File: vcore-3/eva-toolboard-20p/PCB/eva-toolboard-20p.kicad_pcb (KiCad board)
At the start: 2 copper layers, 44.1 x 48.8 mm, 12 parts, among them J1 TH0, J2 HEATER, J3 STEPPER, J4 Main connector, J5 HOTENDFAN, J6 PARTFAN_1, J7 PARTFAN_2, J8 ENDSTOP_X, J9 PROBE

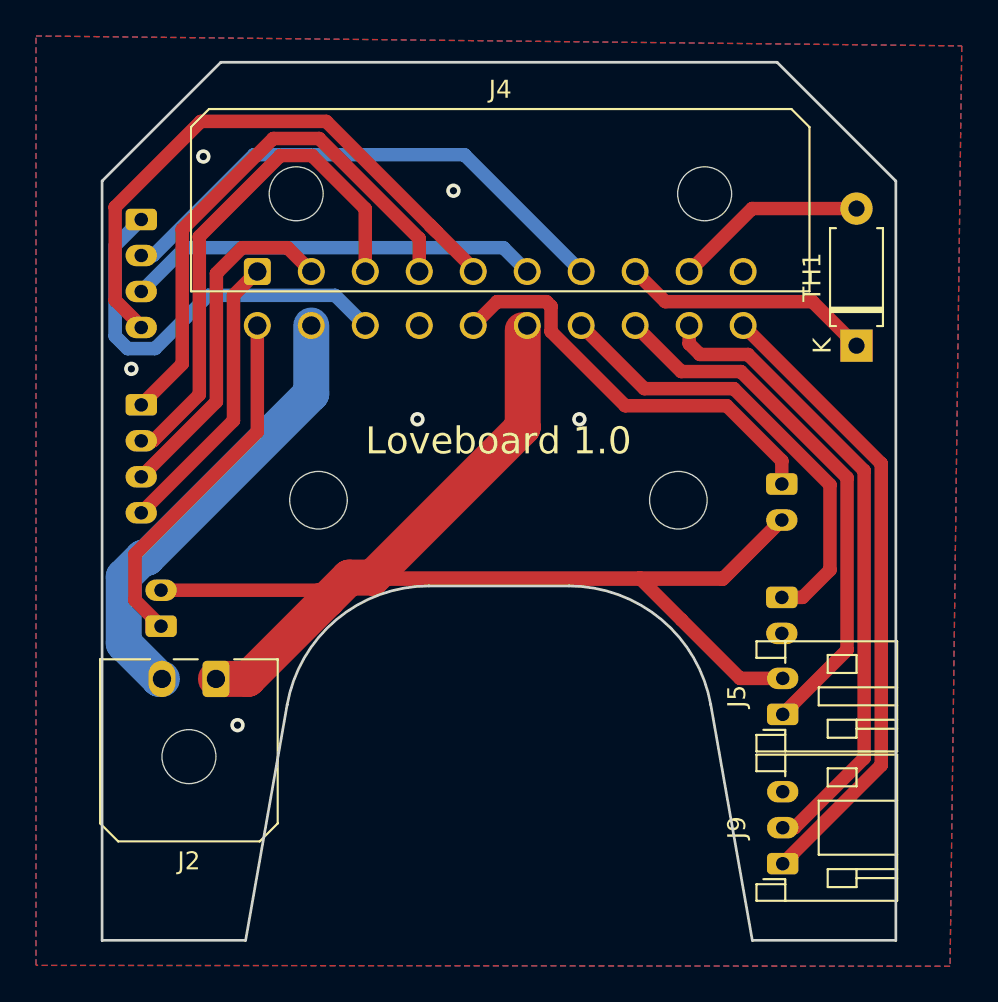
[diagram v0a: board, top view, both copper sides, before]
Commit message: Added and moved connector labels
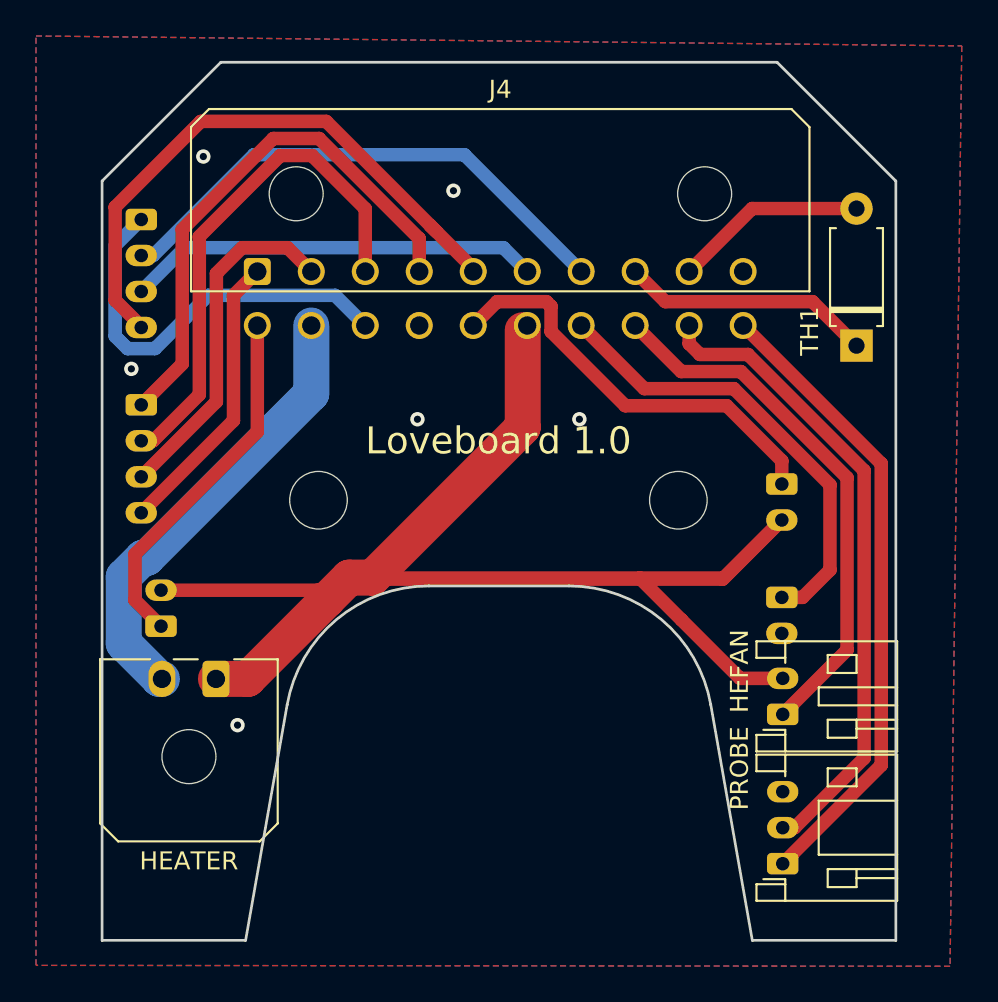
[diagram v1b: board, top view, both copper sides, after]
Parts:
- renumbered J8 to E_X, J2 to HEATER, J5 to HEFAN, J6 to PFAN1, J7 to PFAN2, J9 to PROBE, J3 to STEPPER, J1 to TH0
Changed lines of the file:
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@@
     (property "Sheetname" "")
     (attr through_hole)
-    (fp_text reference "J9" (at 2 -2.55 90) (layer "F.SilkS")
+    (fp_text reference "PROBE" (at 5.3 -2.4 90) (layer "F.SilkS")
       (effects (font (size 1 1) (thickness 0.15)))
     )
@@
     (property "Sheetname" "")
     (attr through_hole)
-    (fp_text reference "J2" (at 1.5 -10.12) (layer "F.SilkS")
+    (fp_text reference "HEATER" (at 1.5 -10.12) (layer "F.SilkS")
       (effects (font (size 1 1) (thickness 0.15)))
     )
@@
     (property "Sheetname" "")
     (attr through_hole)
-    (fp_text reference "TH1" (at 3.81 -2.47 90) (layer "F.SilkS")
+    (fp_text reference "TH1" (at 0.81 -2.6 90) (layer "F.SilkS")
       (effects (font (size 1 1) (thickness 0.15)))
     )
@@
       (effects (font (size 1 1) (thickness 0.15)))
     )
-    (fp_text user "K" (at 0 -1.9 90) (layer "F.SilkS")
-      (effects (font (size 1 1) (thickness 0.15)))
-    )
     (fp_text user "${REFERENCE}" (at 4.2 0 90) (layer "F.Fab")
-      (effects (font (size 1 1) (thickness 0.15)))
-    )
-    (fp_text user "K" (at 0 -1.9 90) (layer "F.Fab")
       (effects (font (size 1 1) (thickness 0.15)))
     )
@@
     (property "Sheetname" "")
     (attr through_hole)
-    (fp_text reference "J5" (at 1 -2.55 90) (layer "F.SilkS")
+    (fp_text reference "HEFAN" (at 2.4 -2.4 90) (layer "F.SilkS")
       (effects (font (size 1 1) (thickness 0.15)))
     )
@@
     (property "Sheetname" "")
     (attr through_hole)
-    (fp_text reference "J7" (at 1 2.9 90) (layer "B.SilkS")
+    (fp_text reference "PFAN2" (at 1 3 90) (layer "B.SilkS")
       (effects (font (size 1 1) (thickness 0.15)) (justify mirror))
     )
@@
     (property "Sheetname" "")
     (attr through_hole)
-    (fp_text reference "J8" (at 1 2.55 90) (layer "B.SilkS")
+    (fp_text reference "E_X" (at 1 2.55 90) (layer "B.SilkS")
       (effects (font (size 1 1) (thickness 0.15)) (justify mirror))
     )
@@
     (property "Sheetname" "")
     (attr through_hole)
-    (fp_text reference "J6" (at 1 2.55 90) (layer "B.SilkS")
+    (fp_text reference "PFAN1" (at -3.35 -2.75 180) (layer "B.SilkS")
       (effects (font (size 1 1) (thickness 0.15)) (justify mirror))
     )
@@
     (property "Sheetname" "")
     (attr through_hole)
-    (fp_text reference "J3" (at 3 2.9 90) (layer "B.SilkS")
+    (fp_text reference "STEPPER" (at 3.1 -4.35 90) (layer "B.SilkS")
       (effects (font (size 1 1) (thickness 0.15)) (justify mirror))
     )
@@
     (property "Sheetname" "")
     (attr through_hole)
-    (fp_text reference "J1" (at 3 2.9 90) (layer "B.SilkS")
-      (effects (font (size 1 1) (thickness 0.15)) (justify mirror))
-    )
+    (fp_text reference "TH0" (at 3 -4.25 90) (layer "B.SilkS")
+      (effects (font (size 1 1) (thickness 0.15)) (justify mirror))
+    )
